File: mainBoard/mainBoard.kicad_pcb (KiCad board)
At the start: 4 copper layers, 118.4 x 54.5 mm, 76 parts, among them J1 Conn_01x01, J10 Conn_01x05, J11 Conn_01x04, J12 Conn_01x01, J13 Conn_01x01, J14 Conn_01x01, J15 Conn_01x01, J16 Conn_01x01, J17 Conn_01x01, J18 Conn_01x01, J19 Conn_01x01, J2 Conn_01x01, J20 Conn_01x01, J21 Conn_01x01, J22 Conn_01x01, J23 Conn_01x05, J24 Conn_01x04, J25 Conn_01x05, J26 Conn_01x05, J27 Conn_01x05, J28 Conn_01x04, J29 Conn_01x04, J3 Conn_01x01, J30 Conn_01x04, J31 Conn_02x05_Odd_Even, J32 Conn_02x07_Odd_Even, J33 Conn_01x04, J34 Conn_01x02, J35 Conn_01x02, J36 Conn_01x03, J37 Conn_01x02, J38 Conn_01x02, J4 Conn_01x01, J5 Conn_01x01, J6 Conn_01x01, J7 Conn_01x01, J8 Conn_01x01, J9 Conn_01x01, M1 Conn_01x01, M2 Conn_01x01, U1 STM32H503CBT6, U2 DRV8251ADDAR, U3 MAX15062A, U4 64Kbit

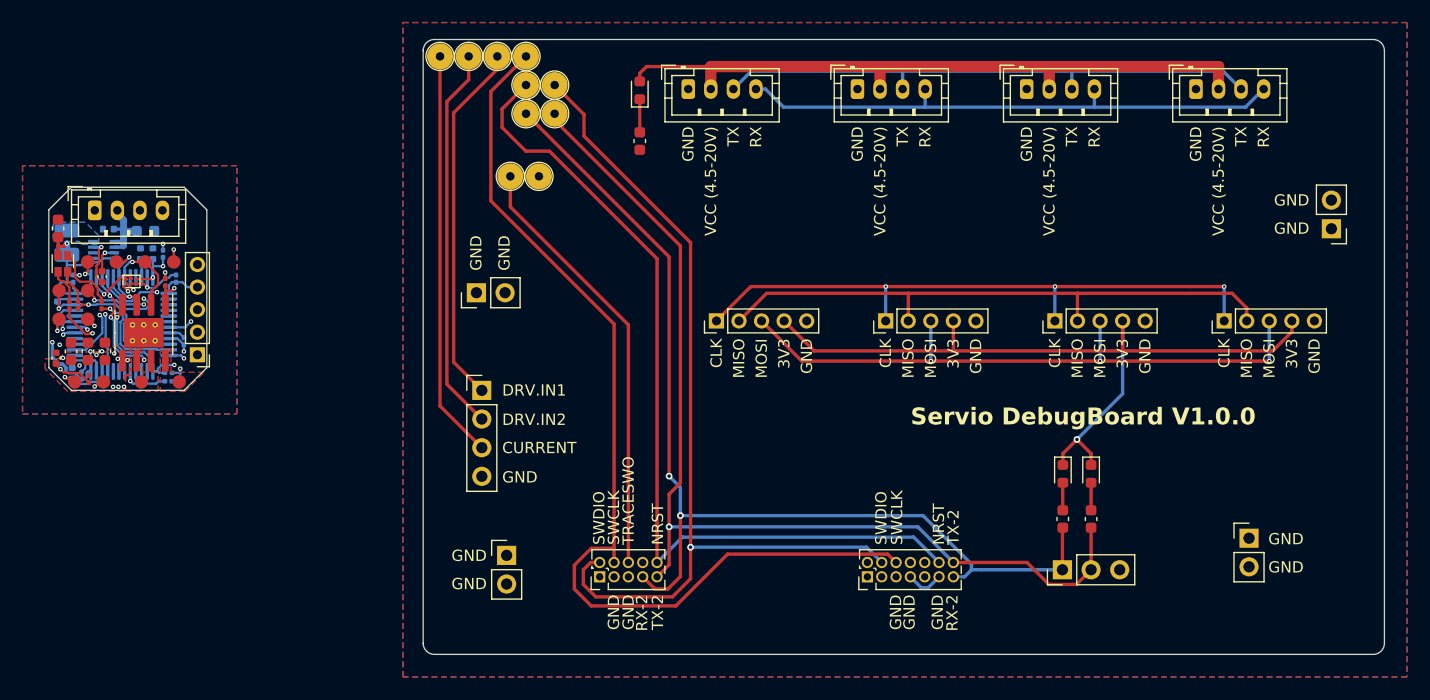
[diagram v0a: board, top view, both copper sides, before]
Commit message: Mounting holes and recessing the main board
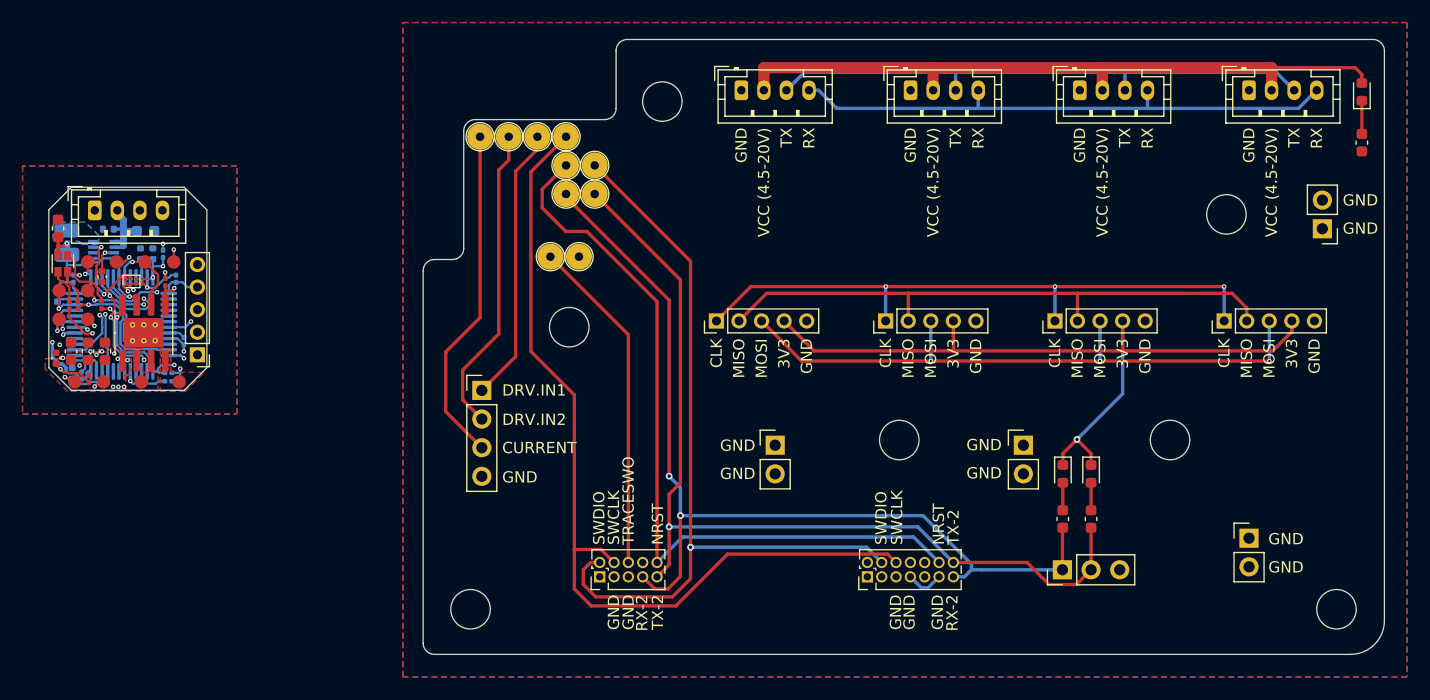
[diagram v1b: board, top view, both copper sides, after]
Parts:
- moved D2 64.0 mm to (210.0, 56.1)
- moved R7 64.0 mm to (210.0, 60.6)
- moved J38 50.3 mm to (180.0, 87.5), turned to 0 degrees
- moved J34 25.7 mm to (158.0, 87.5)
- moved J17 7.96 mm to (139.5, 65.2)
- moved J14 7.96 mm to (139.5, 60.1)
- moved J15 7.96 mm to (139.5, 62.7)
- moved J19 7.96 mm to (136.9, 60.1)
- moved J21 7.96 mm to (131.8, 60.1)
- moved J22 7.96 mm to (140.6, 70.8)
- moved J16 7.96 mm to (142.0, 65.2)
- moved J13 7.96 mm to (142.0, 62.7)
- moved J18 7.96 mm to (134.4, 60.1)
- moved J20 7.96 mm to (138.1, 70.8)
- moved J24 4.71 mm to (155.0, 56.0)
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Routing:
- net /DebuBoard/DB-TUNING-LINES.SWCLK: track 88.3 -> 78.3 mm
- net /DebuBoard/DB-TUNING-LINES.NRST: track 77.0 -> 68.2 mm
- net /DebuBoard/DB-TUNING-LINES.RX-2: track 92.7 -> 84.1 mm
- net /DebuBoard/DB-TUNING-LINES.TRACESWO: track 38.6 -> 30.0 mm
- net /DebuBoard/DB-TUNING-LINES.SWDIO: track 79.9 -> 71.3 mm
- net /DebuBoard/DB-TUNING-LINES.TX-2: track 90.3 -> 82.3 mm
- net /DebuBoard/DB-DRV.IN1: track 32.2 -> 24.5 mm
- net /DebuBoard/DB-DRV.IN2: track 34.2 -> 27.4 mm
- net /DebuBoard/DB-DRV.CURRENT: track 36.2 -> 30.1 mm
- net Net-(D2-A): track 60.2 -> 62.0 mm
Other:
- outline, holes or cut-outs redrawn

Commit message: Corners
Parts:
- moved D2 0.86 mm to (210.0, 57.0)
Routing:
- net Net-(D2-K): track 2.94 -> 2.08 mm
- net Net-(D2-A): track 62.0 -> 62.6 mm
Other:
- outline, holes or cut-outs redrawn
- board text added: "PWR"
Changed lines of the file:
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@@
   )
   (footprint "LED_SMD:LED_0603_1608Metric" (layer "F.Cu")
-    (at 210 56.14375 90)
+    (at 210 57 90)
     (descr "LED SMD 0603 (1608 Metric), square (rectangular) end terminal, IPC_7351 nominal, (Body size source: http://www.tortai-tech.com/upload/download/2011102023233369053.pdf), generated with kicad-footprint-generator")
     (tags "LED")
@@
   (gr_arc (start 143.9 57.6) (mid 143.607107 58.307107) (end 142.9 58.6)
     (stroke (width 0.1) (type default)) (layer "Edge.Cuts"))
-  (gr_line (start 127.8 106) (end 209 106)
+  (gr_line (start 129.799999 106.000001) (end 209 106)
     (stroke (width 0.1) (type default)) (layer "Edge.Cuts"))
   (gr_line (start 129.4 71) (end 127.8 71)
@@
   (gr_line (start 105.625 82.595) (end 95.625 82.595)
     (stroke (width 0.1) (type default)) (layer "Edge.Cuts"))
+  (gr_arc (start 209.000001 51.499999) (mid 211.121321 52.378679) (end 212.000001 54.499999)
+    (stroke (width 0.1) (type default)) (layer "Edge.Cuts"))
   (gr_arc (start 130.4 70) (mid 130.107107 70.707107) (end 129.4 71)
     (stroke (width 0.1) (type default)) (layer "Edge.Cuts"))
   (gr_circle (center 148 57) (end 149.75 57)
     (stroke (width 0.1) (type default)) (fill none) (layer "Edge.Cuts"))
-  (gr_arc (start 211 51.5) (mid 211.707107 51.792893) (end 212 52.5)
-    (stroke (width 0.1) (type default)) (layer "Edge.Cuts"))
   (gr_arc (start 212 103) (mid 211.12132 105.12132) (end 209 106)
     (stroke (width 0.1) (type default)) (layer "Edge.Cuts"))
-  (gr_line (start 211 51.5) (end 144.9 51.5)
+  (gr_line (start 209.000001 51.499999) (end 144.9 51.5)
     (stroke (width 0.1) (type default)) (layer "Edge.Cuts"))
   (gr_circle (center 139.75 77) (end 141.5 77)
@@
   (gr_line (start 95.625 82.595) (end 93.625 80.595)
     (stroke (width 0.1) (type default)) (layer "Edge.Cuts"))
+  (gr_arc (start 129.799999 106.000001) (mid 127.678679 105.121321) (end 126.799999 103.000001)
+    (stroke (width 0.1) (type default)) (layer "Edge.Cuts"))
   (gr_line (start 105.625 64.595) (end 107.625 66.595)
     (stroke (width 0.1) (type default)) (layer "Edge.Cuts"))
-  (gr_line (start 126.8 72) (end 126.8 105)
+  (gr_line (start 126.8 72) (end 126.799999 103.000001)
     (stroke (width 0.1) (type default)) (layer "Edge.Cuts"))
   (gr_line (start 130.4 70) (end 130.4 59.6)
@@
     (stroke (width 0.1) (type default)) (layer "Edge.Cuts"))
   (gr_arc (start 143.9 52.5) (mid 144.192893 51.792893) (end 144.9 51.5)
-    (stroke (width 0.1) (type default)) (layer "Edge.Cuts"))
-  (gr_arc (start 127.8 106) (mid 127.092893 105.707107) (end 126.8 105)
     (stroke (width 0.1) (type default)) (layer "Edge.Cuts"))
   (gr_circle (center 193 87) (end 194.75 87)
@@
   (gr_circle (center 169 87) (end 170.75 87)
     (stroke (width 0.1) (type default)) (fill none) (layer "Edge.Cuts"))
-  (gr_line (start 212 103) (end 212 52.5)
+  (gr_line (start 212 103) (end 212.000001 54.499999)
     (stroke (width 0.1) (type default)) (layer "Edge.Cuts"))
   (gr_line (start 107.625 80.595) (end 105.625 82.595)
@@
     (effects (font (size 1 1) (thickness 0.15)) (justify right))
   )
+  (gr_text "RX-2" (at 183.6 100.3 90) (layer "F.SilkS")
+    (effects (font (size 1 1) (thickness 0.15)) (justify right))
+  )
+  (gr_text "TX-2" (at 186 100.3 90) (layer "F.SilkS")
+    (effects (font (size 1 1) (thickness 0.15)) (justify right))
+  )
   (gr_text "GND" (at 153.105 89.99) (layer "F.SilkS")
     (effects (font (size 1 1) (thickness 0.15)) (justify left))
@@
     (effects (font (size 1 1) (thickness 0.15)) (justify right))
   )
+  (gr_text "PWR" (at 210 52.1 90) (layer "F.SilkS")
+    (effects (font (size 1 1) (thickness 0.15)) (justify right))
+  )
   (gr_text "3V3" (at 173.8 78 90) (layer "F.SilkS")
     (effects (font (size 1 1) (thickness 0.15)) (justify right))
@@
     (effects (font (size 1 1) (thickness 0.15)) (justify right))
   )
+  (gr_text "GND" (at 188.6 100.3 90) (layer "F.SilkS")
+    (effects (font (size 1 1) (thickness 0.15)) (justify right))
+  )
+  (gr_text "TX-2" (at 185.9 84.1 90) (layer "F.SilkS")
+    (effects (font (size 1 1) (thickness 0.15)) (justify right))
+  )
   (gr_text "3V3" (at 203.8 78 90) (layer "F.SilkS")
     (effects (font (size 1 1) (thickness 0.15)) (justify right))
@@
   )
   (gr_text "GND" (at 155.005 59.305 90) (layer "F.SilkS")
+    (effects (font (size 1 1) (thickness 0.15)) (justify right))
+  )
+  (gr_text "RX-2" (at 183.5 84.1 90) (layer "F.SilkS")
     (effects (font (size 1 1) (thickness 0.15)) (justify right))
   )
@@
   (segment (start 143.72 97.855) (end 142.565 96.7) (width 0.3) (layer "F.Cu") (net 52))
   (segment (start 141.7 101.7) (end 140.2 100.2) (width 0.3) (layer "F.Cu") (net 52))
-  (segment (start 141.32 68.52) (end 147.53 74.73) (width 0.3) (layer "F.Cu") (net 53))
-  (segment (start 137.35 66.42) (end 139.45 68.52) (width 0.3) (layer "F.Cu") (net 53))
+  (segment (start 137.35 66.42) (end 138.73 67.8) (width 0.3) (layer "F.Cu") (net 53))
+  (segment (start 140.3 67.8) (end 147.53 75.03) (width 0.3) (layer "F.Cu") (net 53))
+  (segment (start 138.73 67.8) (end 140.3 67.8) (width 0.3) (layer "F.Cu") (net 53))
+  (segment (start 147.53 75.03) (end 147.53 97.855) (width 0.3) (layer "F.Cu") (net 53))
   (segment (start 139.465 62.66) (end 137.35 64.775) (width 0.3) (layer "F.Cu") (net 53))
-  (segment (start 139.45 68.52) (end 141.32 68.52) (width 0.3) (layer "F.Cu") (net 53))
   (segment (start 137.35 64.775) (end 137.35 66.42) (width 0.3) (layer "F.Cu") (net 53))
-  (segment (start 147.53 74.73) (end 147.53 97.855) (width 0.3) (layer "F.Cu") (net 53))
   (segment (start 149.785 95.6) (end 147.53 97.855) (width 0.3) (layer "B.Cu") (net 53))
   (segment (start 170.27 95.6) (end 149.785 95.6) (width 0.3) (layer "B.Cu") (net 53))
@@
   (segment (start 176 57.6) (end 176.005 57.605) (width 0.3) (layer "B.Cu") (net 66))
   (segment (start 191.005 57.605) (end 176.005 57.605) (width 0.3) (layer "B.Cu") (net 66))
-  (segment (start 210 59.86875) (end 210 56.93125) (width 0.3) (layer "F.Cu") (net 76))
+  (segment (start 210 59.86875) (end 210 57.7875) (width 0.3) (layer "F.Cu") (net 76))
   (segment (start 172 56) (end 172 54.01) (width 1) (layer "F.Cu") (net 77))
   (segment (start 157 54.01) (end 157.005 54.005) (width 1) (layer "F.Cu") (net 77))
-  (segment (start 202.005 54.005) (end 209.405 54.005) (width 0.3) (layer "F.Cu") (net 77))
   (segment (start 157 56) (end 157 54.01) (width 1) (layer "F.Cu") (net 77))
-  (segment (start 209.405 54.005) (end 210 54.6) (width 0.3) (layer "F.Cu") (net 77))
+  (segment (start 210 55) (end 210 56.2125) (width 0.3) (layer "F.Cu") (net 77))
   (segment (start 187 56) (end 187 54.01) (width 1) (layer "F.Cu") (net 77))
   (segment (start 202 54.01) (end 202 56) (width 1) (layer "F.Cu") (net 77))
-  (segment (start 210 54.6) (end 210 55.35625) (width 0.3) (layer "F.Cu") (net 77))
   (segment (start 172.005 54.005) (end 187.005 54.005) (width 1) (layer "F.Cu") (net 77))
   (segment (start 187.005 54.005) (end 202.005 54.005) (width 1) (layer "F.Cu") (net 77))
+  (segment (start 202.005 54.005) (end 209.005 54.005) (width 0.3) (layer "F.Cu") (net 77))
+  (segment (start 209.005 54.005) (end 210 55) (width 0.3) (layer "F.Cu") (net 77))
   (segment (start 172 54.01) (end 172.005 54.005) (width 1) (layer "F.Cu") (net 77))
   (segment (start 157.005 54.005) (end 172.005 54.005) (width 1) (layer "F.Cu") (net 77))

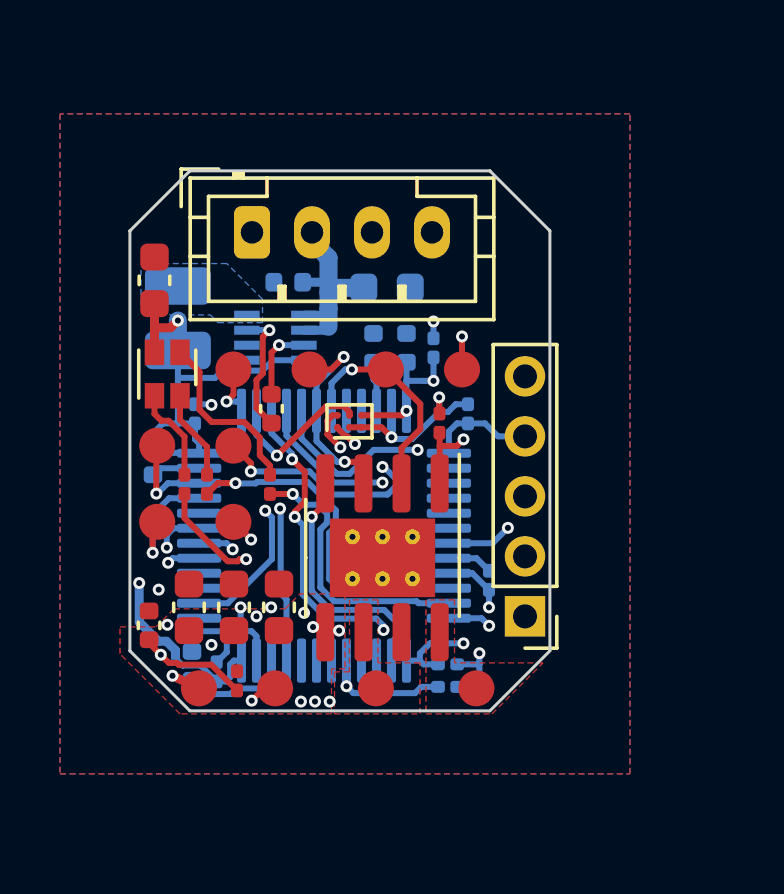
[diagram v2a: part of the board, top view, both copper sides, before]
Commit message: Add GND via for better cooling
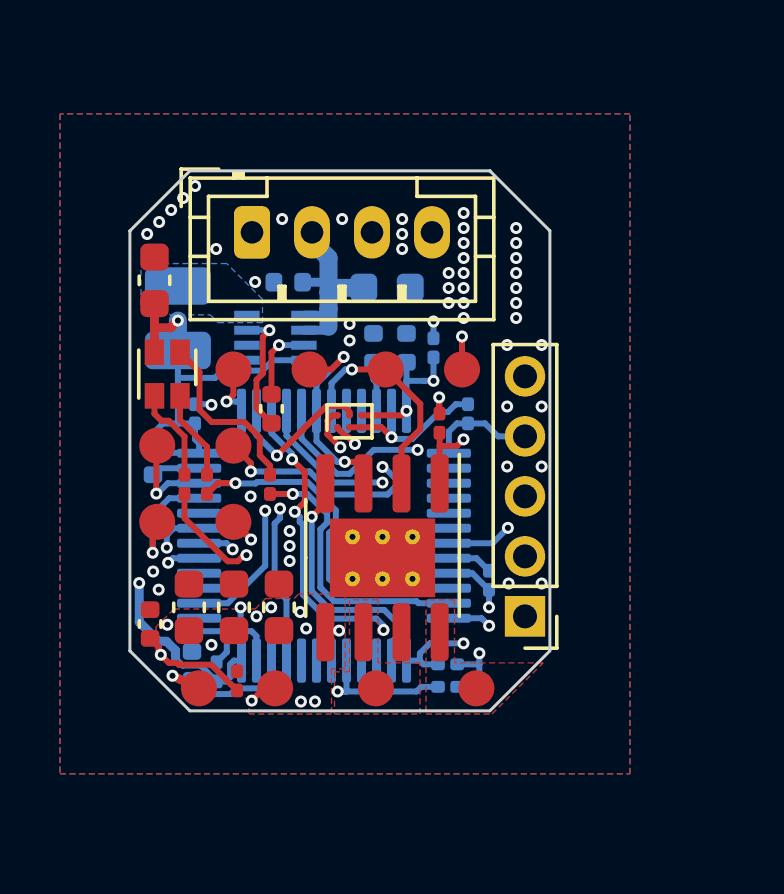
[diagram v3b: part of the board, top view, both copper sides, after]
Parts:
- moved C18 0.06 mm to (94.3, 79.7)
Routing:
- net GND: vias 9 -> 54
- net /MotorBoard/VCC: vias 10 -> 9

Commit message: Bigger via
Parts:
- moved C2 0.20 mm to (105.1, 72.7)
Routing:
- net /MotorBoard/CPU/ENC.CLK: track 18.9 -> 15.1 mm
- net /MotorBoard/CPU/LED.G: track 21.8 -> 20.1 mm
- net /MotorBoard/CPU/EEPROM.SDA: track 10.7 -> 11.7 mm
- net /MotorBoard/TUNING-LINES.NRST: track 14.5 -> 15.2 mm
- net GND: track 27.5 -> 27.8 mm, vias 54 -> 53
- net /MotorBoard/VCC: vias 9 -> 8

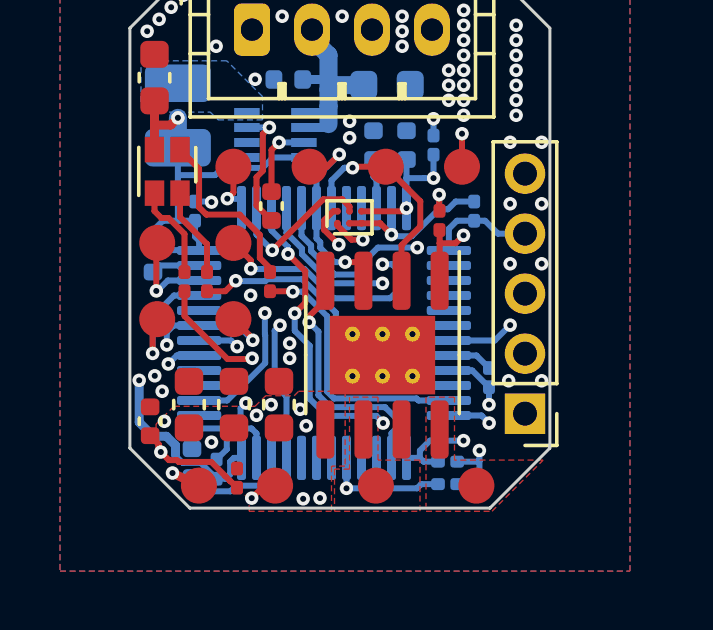
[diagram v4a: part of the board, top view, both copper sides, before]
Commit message: SDA pullup add to PCB
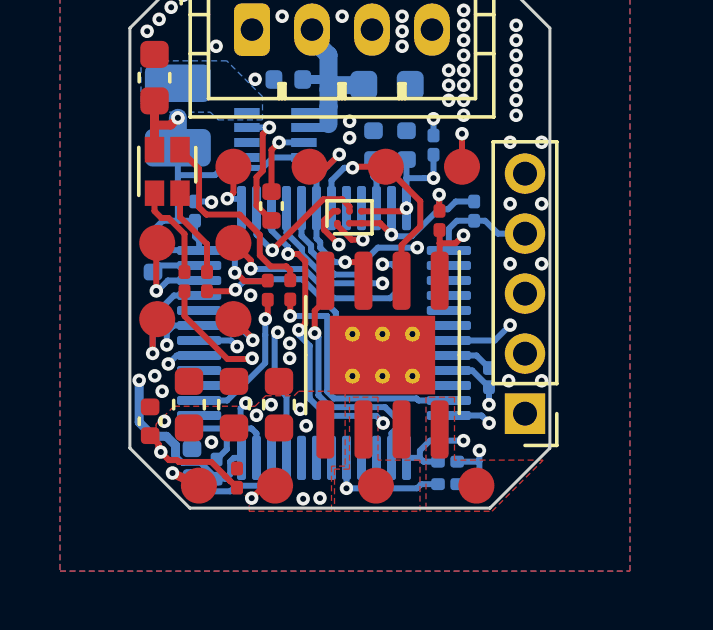
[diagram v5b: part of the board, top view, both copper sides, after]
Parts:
- added R10: 10k, Resistor_SMD:R_0201_0603Metric, F.Cu at (98.2, 75.3)
- moved R6 0.73 mm to (99.0, 75.3)
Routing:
- net VDD: track 72.4 -> 75.3 mm, vias 5 -> 6
- net Net-(D1-BK): track 5.97 -> 6.83 mm
- net /MotorBoard/CPU/EEPROM.SDA: track 11.7 -> 12.4 mm

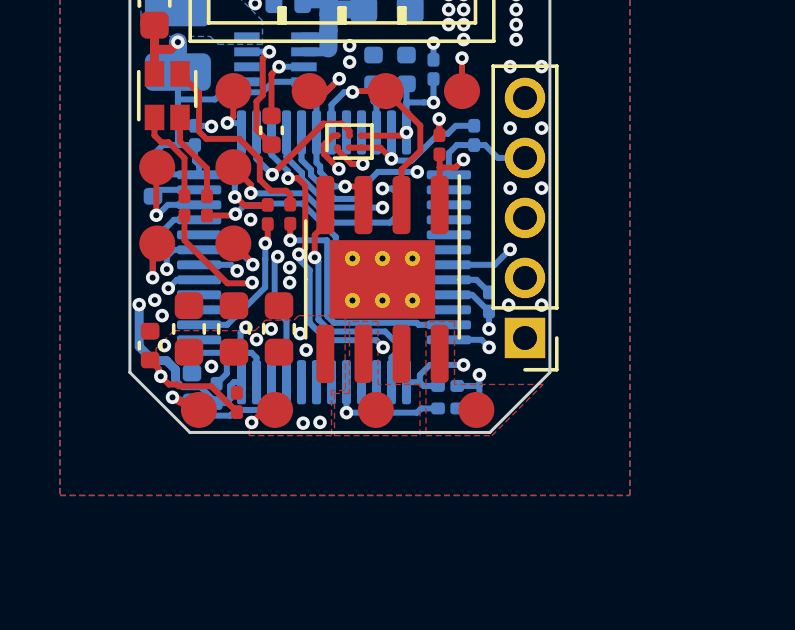
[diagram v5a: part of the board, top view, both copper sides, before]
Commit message: Change pin configuration for encoder header
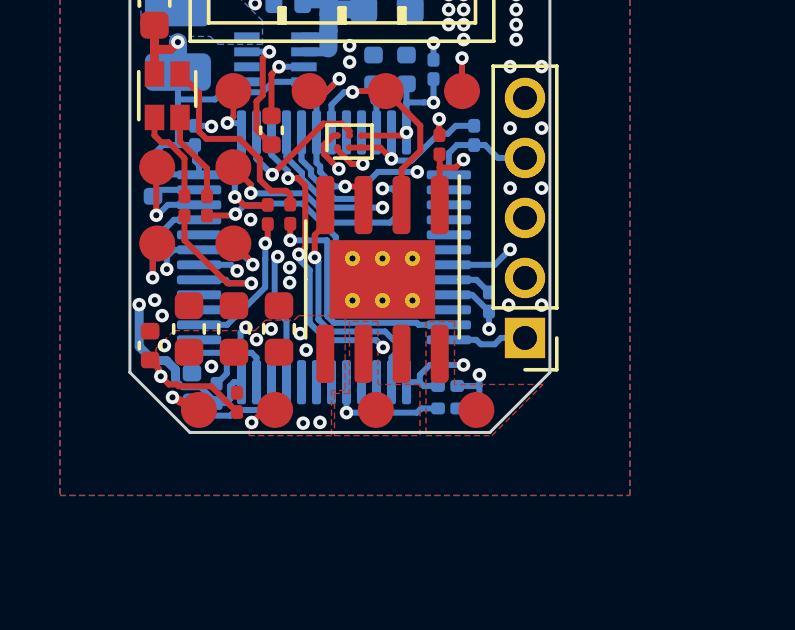
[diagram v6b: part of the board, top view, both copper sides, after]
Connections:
- net GND renamed VSS
- U1 pad 12: /MotorBoard/CPU/LED.G -> /MotorBoard/CPU/ENC.CLK
- U1 pad 29: /MotorBoard/CPU/ENC.CLK -> /MotorBoard/CPU/LED.G
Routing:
- net /MotorBoard/CPU/LED.G: track 20.1 -> 5.44 mm, vias 2 -> 1
- net /MotorBoard/CPU/ENC.CLK: track 15.1 -> 2.69 mm, vias 1 -> 0
